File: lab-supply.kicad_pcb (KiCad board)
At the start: 2 copper layers, 94 x 66 mm, 38 parts, among them Q1 Q_NPN_BCE, U1 AD8208, U2 MAX1719EUT, U3 MP8862GQ, U4 MCP4716AxT-ECH, U5 LM4040DBZ-2.5, U6 MCP4716AxT-ECH

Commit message: Kept working on the design
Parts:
- removed the C7 at (118.9, 93.5)
- removed the R5 at (127.4, 72.1)
- removed TP4: Mount Hole, Connector_PinHeader_2.54mm:PinHeader_1x04_P2.54mm_Vertical
- removed U4, U6: MCP4716AxT-ECH, Package_TO_SOT_SMD:SOT-23-6_Handsoldering
- removed U5: LM4040DBZ-2.5, Package_TO_SOT_SMD:SOT-23
- added C10: 22u, Rays Footprints:C_1210_HandSoldering, F.Cu at (136.7, 95.5)
- added C11: 22u, Rays Footprints:C_1210_HandSoldering, F.Cu at (140.4, 95.5)
- added C15: 100u, Capacitor_SMD:CP_Elec_6.3x5.9, F.Cu at (143.5, 88.6)
- added C16: 0.1u, Rays Footprints:C_0603_HandSoldering, F.Cu at (148.8, 89.5)
- added C8: 22u, Rays Footprints:C_1210_HandSoldering, F.Cu at (114.4, 93.3)
- added R6: 300k, Rays Footprints:R_0805_HandSoldering, F.Cu at (124.2, 78.6)
- added R7: 0, Rays Footprints:R_0805_HandSoldering, F.Cu at (130.4, 91.7)
- added R8: 0, Rays Footprints:R_0805_HandSoldering, F.Cu at (124.4, 96.1)
- C12, C13: value 0.1u -> 22u; footprint Rays Footprints:C_0603_HandSoldering -> Rays Footprints:C_1210_HandSoldering
- TP1: value Mount Hole -> Input Power
- TP2: value Mount Hole -> Output Power
- TP3: footprint Connector_PinHeader_2.54mm:PinHeader_1x10_P2.54mm_Vertical -> Connector_PinHeader_2.54mm:PinHeader_1x07_P2.54mm_Vertical
- moved C12 30.3 mm to (144.0, 95.5), turned to 90 degrees
- moved C13 27.1 mm to (147.6, 95.5), turned to 270 degrees
- moved TP3 9.92 mm to (157.1, 69.3)
- moved R9 6.57 mm to (131.1, 102.7), turned to 180 degrees
- moved C9 6.46 mm to (120.0, 79.1), turned to 270 degrees
- moved R5 6.35 mm to (122.8, 91.7)
- moved TP2 6.35 mm to (157.1, 91.7)
- moved U2 6.22 mm to (122.9, 84.3)
- moved C14 5.43 mm to (137.2, 89.4), turned to 90 degrees
- moved Q1 1.27 mm to (131.2, 98.0)
- moved TP1 1.27 mm to (87.5, 102.1)
- moved C17 0.76 mm to (122.3, 98.2)
- moved C18 0.76 mm to (120.9, 102.6)
- moved C19 0.76 mm to (126.2, 98.2)
- moved U3 0.76 mm to (123.8, 102.6)
- renumbered C5 to C1, C11 to C14, C15 to C17, C2 to C18, C3 to C19, C6 to C2, C1 to C3, C9 to C5, C10 to C6, C8 to C7, C14 to C9, R2 to R1, R3 to R2, R1 to R3, R11 to R5, R6 to R9, U3 to U1, U1 to U2, U2 to U3
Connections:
- C12 pad 2: +5V -> VOUT
- C13 pad 1: GND -> VOUT
- C13 pad 2: VREF_2.5 -> GND
- C14 pad 1: Net-(C11-Pad1) -> VOUT
- C17 pad 1: +5V -> Net-(C17-Pad1)
- Q1 pad 3: Net-(C11-Pad1) -> VOUT
- R3 pad 2: BB_ALT -> BB_ALERT
- R5 pad 1: Net-(C11-Pad1) -> Net-(R5-Pad1)
- R9 pad 1: -5V -> Net-(Q1-Pad2)
- R9 pad 2: Net-(Q1-Pad2) -> -5V
- TP2 pad 1: Net-(C11-Pad1) -> VOUT
- TP2 pad 2: Net-(C11-Pad1) -> VOUT
- TP2 pad 3: Net-(C11-Pad1) -> VOUT
- TP3 pad 2: DAC1_SCL -> VOUT
- TP3 pad 3: DAC1_SDA -> BB_IOUT
- TP3 pad 4: DAC2_SCL -> BB_ALERT
- TP3 pad 5: DAC2_SDA -> SDA
- TP3 pad 6: BB_IOUT -> SCL
- TP3 pad 7: BB_ALT -> GND
- U1 pad 5: BB_SCL -> SCL
- U1 pad 6: BB_SDA -> SDA
- U1 pad 8: BB_ALT -> BB_ALERT
- U2 pad 1: Net-(C11-Pad1) -> Net-(R5-Pad1)
- U3 pad 2: +5V -> Net-(C17-Pad1)
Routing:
- net SDA: track 0.00 -> 93.6 mm, vias 0 -> 2
- net SCL: track 0.00 -> 87.6 mm, vias 0 -> 2
- net BB_ALERT: track 0.00 -> 86.4 mm, vias 0 -> 2
- net BB_SDA: track 77.4 -> 0.00 mm, vias 1 -> 0
- net BB_ALT: track 77.2 -> 0.00 mm, vias 1 -> 0
- net BB_SCL: track 76.8 -> 0.00 mm, vias 1 -> 0
- net Net-(C11-Pad1): track 34.6 -> 0.00 mm
- net VOUT: track 0.00 -> 28.6 mm
- net VOUT_DAC2: track 25.3 -> 0.00 mm, vias 2 -> 0
- net DAC2_SCL: track 22.1 -> 0.00 mm
- net DAC2_SDA: track 21.5 -> 0.00 mm
- net VREF_2.5: track 21.2 -> 0.00 mm
- net DAC1_SCL: track 19.1 -> 0.00 mm
- net DAC1_SDA: track 18.5 -> 0.00 mm
- net VOUT_DAC1: track 14.9 -> 0.00 mm, vias 1 -> 0
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- added copper zone on F.Cu, net -5V
- added copper zone on F.Cu, net Net-(C17-Pad1)
- added copper zone on F.Cu, net Net-(R5-Pad1)
- added copper zone on F.Cu, net VOUT
- removed copper zone on F.Cu, net Net-(C11-Pad1)
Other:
- board text added: "ALERT"
- board text added: "IOUT"
- board text added: "SCL"
- board text added: "SDA"
- board text added: "VOUT"
- board text removed: "BB_ALT"
- board text removed: "BB_IOUT"
- board text removed: "BB_SCL"
- board text removed: "BB_SDA"
- board text removed: "DAC1"
- board text removed: "DAC1_SCL"
- board text removed: "DAC1_SDA"
- board text removed: "DAC2"
- board text removed: "DAC2_SCL"
- board text removed: "DAC2_SDA"

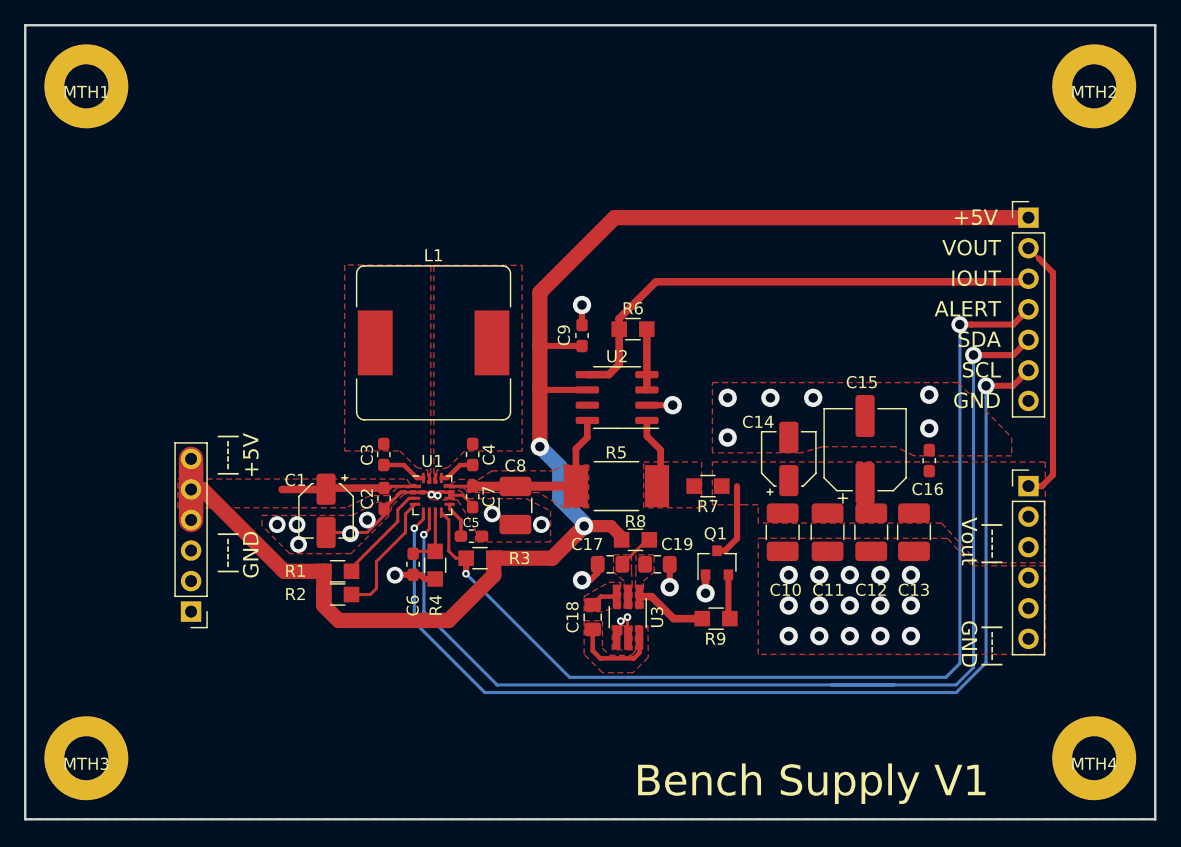
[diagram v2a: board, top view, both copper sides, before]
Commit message: More work on board layouts
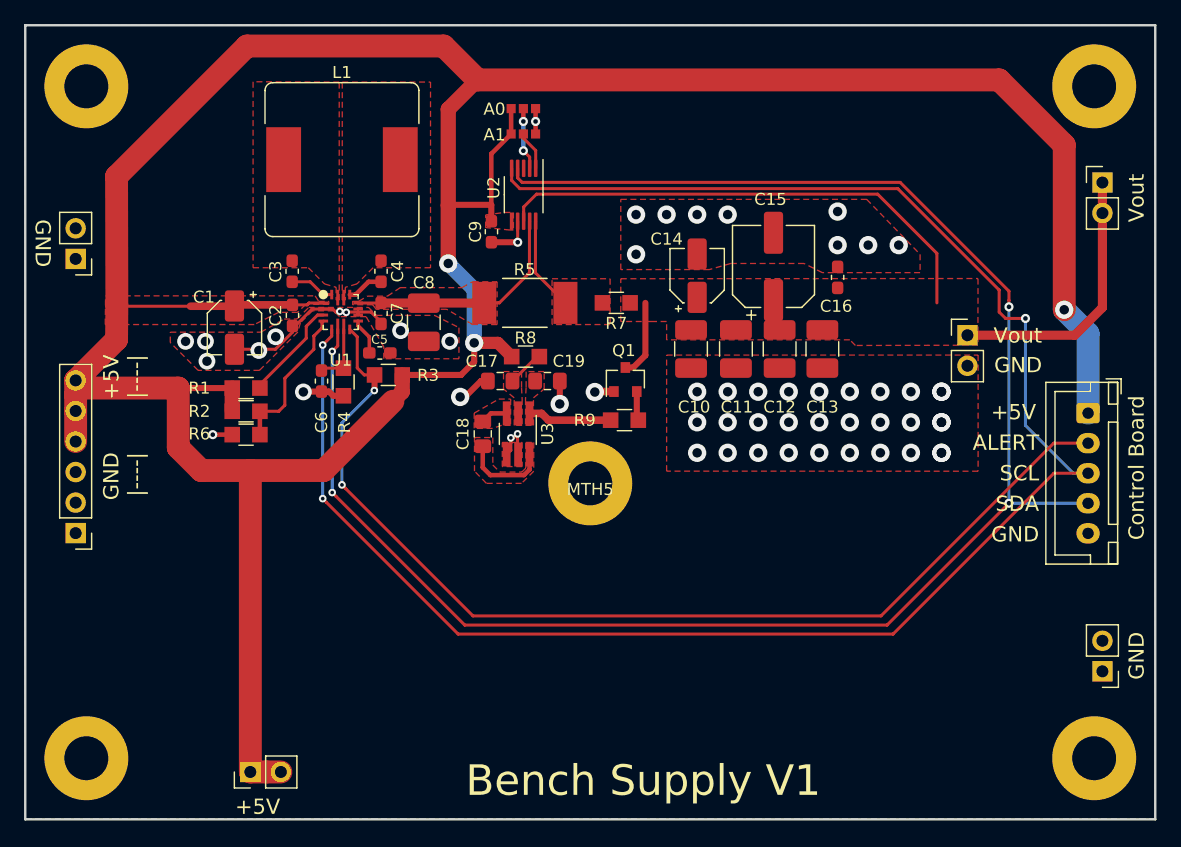
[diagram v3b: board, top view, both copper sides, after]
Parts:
- added JP1: Jumper, Rays Footprints:SolderJumper_3_Pad, F.Cu at (115.1, 62.4)
- added JP2: Jumper, Rays Footprints:SolderJumper_3_Pad, F.Cu at (115.1, 60.3)
- added MTH5: Mount Hole, Rays Footprints:Mount-Hole-#6, F.Cu at (120.7, 91.4)
- added TP4: 0.1" Header, Connector_PinHeader_2.54mm:PinHeader_1x02_P2.54mm_Vertical, F.Cu at (77.9, 72.8)
- added TP5: 0.1" Header, Connector_PinHeader_2.54mm:PinHeader_1x02_P2.54mm_Vertical, F.Cu at (92.4, 115.4)
- added TP6: Output Power, Connector_PinHeader_2.54mm:PinHeader_1x02_P2.54mm_Vertical, F.Cu at (163.2, 107.1)
- added TP7: Power Debug, Connector_PinHeader_2.54mm:PinHeader_1x02_P2.54mm_Vertical, F.Cu at (163.2, 66.4)
- R6: value 300k -> DNP
- TP2: value Output Power -> GND Debug; footprint Connector_PinHeader_2.54mm:PinHeader_1x06_P2.54mm_Vertical -> Connector_PinHeader_2.54mm:PinHeader_1x02_P2.54mm_Vertical
- TP3: footprint Connector_PinHeader_2.54mm:PinHeader_1x07_P2.54mm_Vertical -> Connector_JST:JST_XH_B5B-XH-A_1x05_P2.50mm_Vertical
- U1: footprint Package_DFN_QFN:QFN-16-1EP_3x3mm_P0.5mm_EP1.45x1.45mm -> Rays Footprints:MP8862GQ
- U2: value AD8208 -> INA220; footprint Package_SO:SOIC-8_3.9x4.9mm_P1.27mm -> Package_SO:VSSOP-10_3x3mm_P0.5mm
- moved R6 33.4 mm to (92.0, 87.4), turned to 180 degrees
- moved U2 18.6 mm to (115.1, 67.4), turned to 270 degrees
- moved R9 18.2 mm to (123.5, 86.2)
- moved C17 17.8 mm to (113.2, 82.9)
- moved C18 17.8 mm to (111.7, 87.3)
- moved C19 17.8 mm to (117.1, 82.9)
- moved R8 17.8 mm to (115.3, 80.9)
- moved U3 17.8 mm to (114.6, 87.3)
- moved C12 17.0 mm to (136.4, 80.3)
- moved C13 17.0 mm to (140.0, 80.3)
- moved C16 17.0 mm to (141.2, 74.3)
- moved C6 17.0 mm to (98.3, 82.9)
- moved R1 17.0 mm to (92.0, 83.5)
- moved R4 17.0 mm to (100.1, 83.0)
- moved C1 17.0 mm to (91.1, 78.5)
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- renumbered MTH1 to e
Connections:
- R6 pad 1: BB_IOUT -> Net-(R2-Pad1)
- R6 pad 2: Net-(R6-Pad2) -> GND
- TP2 pad 2: VOUT -> GND
- TP3 pad 2: VOUT -> BB_ALERT
- TP3 pad 3: BB_IOUT -> SCL
- TP3 pad 4: BB_ALERT -> SDA
- TP3 pad 5: SDA -> GND
- U2 pad 1: Net-(R5-Pad1) -> Net-(JP1-Pad2)
- U2 pad 2: GND -> Net-(JP2-Pad2)
- U2 pad 3: Net-(R6-Pad2) -> (no net)
- U2 pad 4: Net-(R6-Pad2) -> SDA
- U2 pad 5: BB_IOUT -> SCL
- U2 pad 7: (no net) -> GND
- U2 pad 8: Net-(C7-Pad2) -> VOUT
- e pad 1: (no net) -> GND
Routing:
- net +5V: track 134.3 -> 271.0 mm, vias 2 -> 3
- net SCL: track 87.6 -> 153.6 mm, vias 2 -> 3
- net SDA: track 93.6 -> 148.6 mm, vias 2 -> 4
- net VOUT: track 28.6 -> 71.2 mm
- net BB_IOUT: track 42.2 -> 0.00 mm
- net Net-(R6-Pad2): track 5.06 -> 0.00 mm
- net Net-(JP2-Pad2): track 0.00 -> 4.80 mm, vias 0 -> 2
- net GND: track 31.6 -> 35.7 mm, vias 38 -> 57
- net Net-(C7-Pad2): track 16.2 -> 19.6 mm
- net Net-(JP1-Pad2): track 0.00 -> 3.28 mm
- net Net-(R2-Pad1): track 10.6 -> 12.6 mm
- net BB_ALERT: track 86.4 -> 88.3 mm
- net Net-(R5-Pad1): track 6.06 -> 7.83 mm
- net -5V: track 5.47 -> 6.98 mm
- net Net-(Q1-Pad2): track 3.70 -> 2.43 mm
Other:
- net class Default: via_dia 1.397 -> 0.762; via_drill 0.7874 -> 0.381
- rule pad_to_mask_clearance: 0.2032 -> 0.0508
- rule solder_mask_min_width: 0.254 -> 0.2032
- board text added: "+5V |----|"
- board text added: "A0"
- board text added: "A1"
- board text added: "Control Board"
- board text added: "GND |----|"
- board text added: "Vout"
- board text removed: "IOUT"
- board text removed: "VOUT"
- board text removed: "|----| +5V"
- board text removed: "|----| GND"
- board text removed: "|----| Vout"

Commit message: Separated Vcc_bb from 5V
Allows for buck/boost to run off of separate Vin from the rest of the circuit. For example +12V
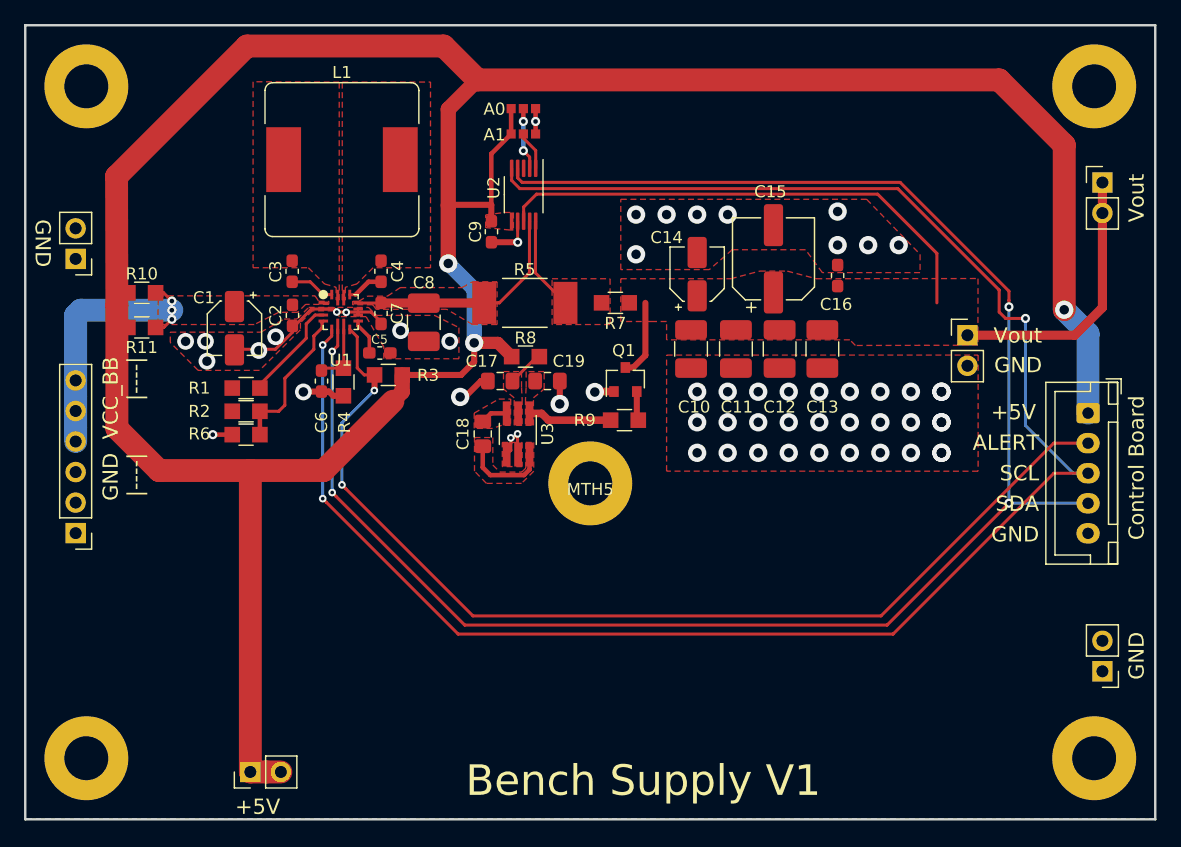
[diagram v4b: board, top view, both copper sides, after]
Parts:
- added R10: 0, Rays Footprints:R_0805_HandSoldering, F.Cu at (83.4, 75.6)
- added R11: 0, Rays Footprints:R_0805_HandSoldering, F.Cu at (83.4, 78.5)
- moved C15 0.64 mm to (135.9, 72.8)
- moved C16 0.15 mm to (141.2, 74.2)
- moved C14 0.13 mm to (129.5, 74.0)
- moved R7 0.08 mm to (122.7, 76.4)
- moved C1 0.05 mm to (91.1, 78.5)
- renumbered e to MTH1
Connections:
- C1 pad 1: +5V -> VCC_BB
- C2 pad 2: +5V -> VCC_BB
- MTH1 pad 1: GND -> (no net)
- R1 pad 2: +5V -> Net-(C5-Pad2)
- R2 pad 2: +5V -> Net-(C5-Pad2)
- TP1 pad 4: +5V -> VCC_BB
- TP1 pad 5: +5V -> VCC_BB
- TP1 pad 6: +5V -> VCC_BB
- U1 pad 1: +5V -> VCC_BB
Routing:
- net +5V: track 271.0 -> 236.9 mm
- net VCC_BB: track 0.00 -> 22.6 mm, vias 0 -> 3
- added copper zone on F.Cu, net VCC_BB
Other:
- board text added: "VCC_BB |----|"
- board text removed: "+5V |----|"
